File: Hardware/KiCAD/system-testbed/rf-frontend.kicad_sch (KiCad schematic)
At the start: 42 parts

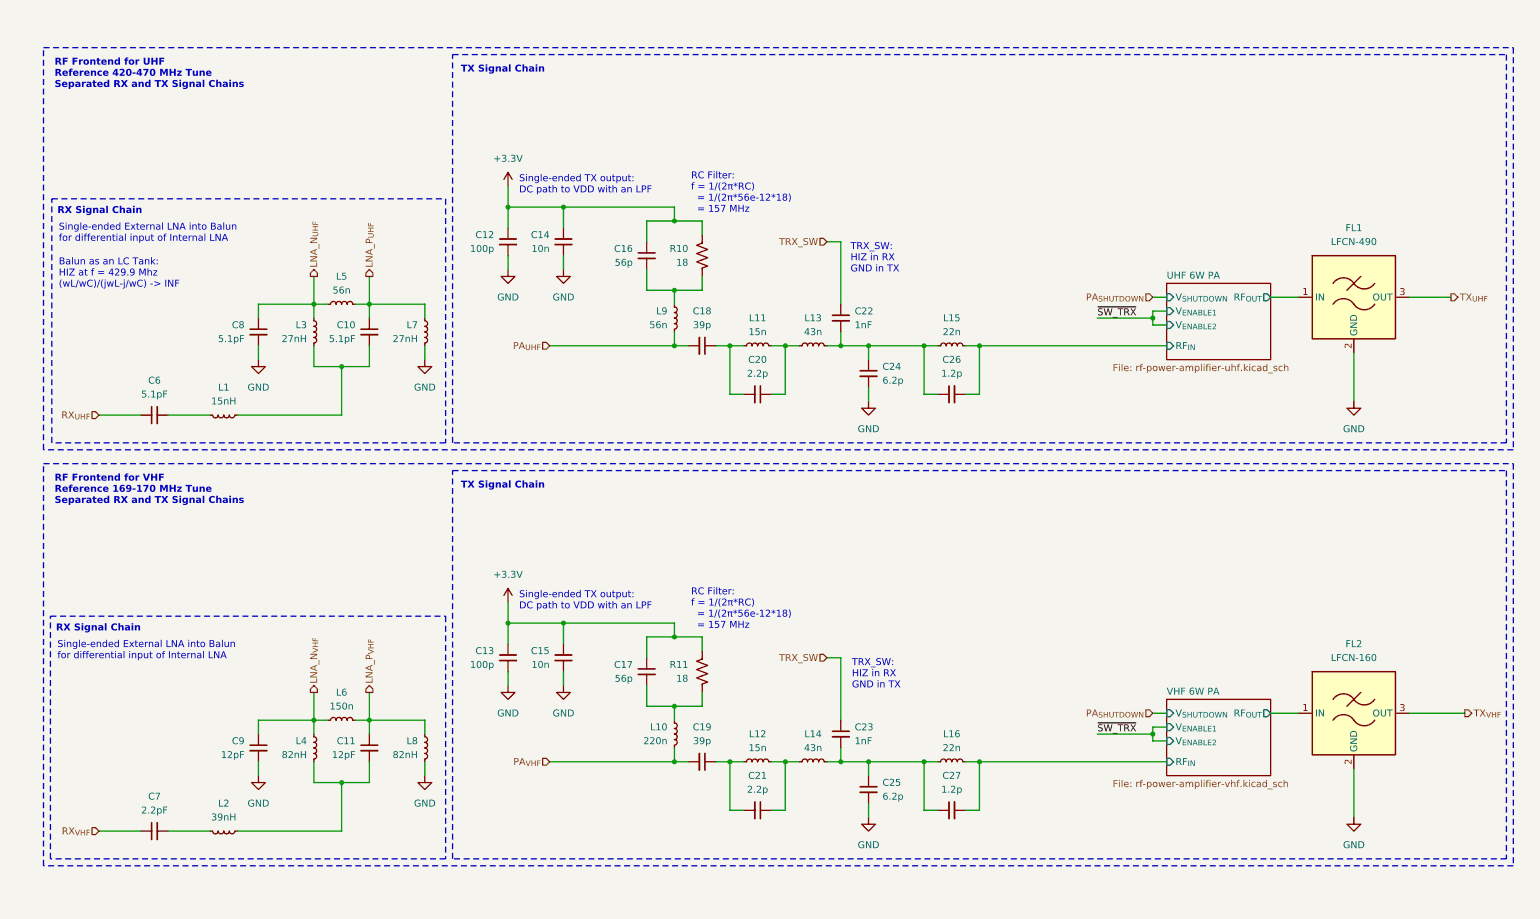
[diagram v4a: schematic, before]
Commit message: feat: separate RF subsystems for testing using SMA edge launches in testbed KiCAD project #65 #34 #45
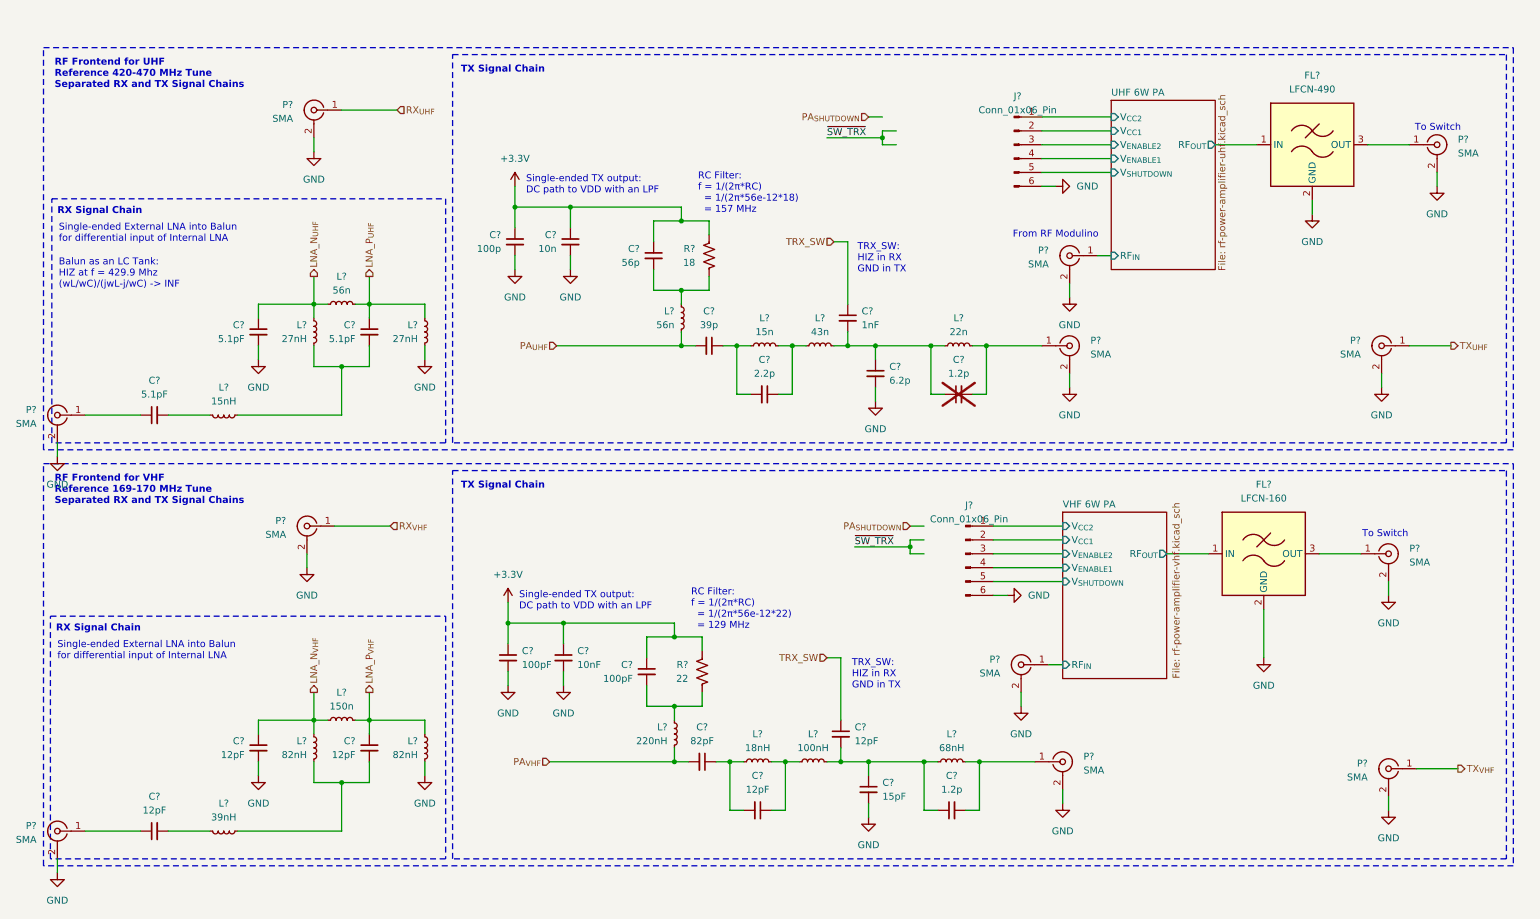
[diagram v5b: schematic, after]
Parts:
- added J? (x2): Conn_01x06_Pin, Connector_PinHeader_2.54mm:PinHeader_1x06_P2.54mm_Vertical, symbol Connector:Conn_01x06_Pin
- added P? (x12): SMA, Connector_Coaxial:SMA_Molex_73251-1153_EdgeMount_Horizontal, symbol Connector:Conn_Coaxial
- C?: renamed from C26; now not fitted
- C?: renamed from C19; value 39p -> 82pF
- C?: renamed from C17; value 56p -> 100pF
- C?: renamed from C21; value 2.2p -> 12pF
- C?: renamed from C15; value 10n -> 10nF
- C?: renamed from C7; value 2.2pF -> 12pF
- C?: renamed from C13; value 100p -> 100pF
- C?: renamed from C25; value 6.2p -> 15pF
- C?: renamed from C23; value 1nF -> 12pF
- C?: renamed from C6; footprint Capacitor_SMD:C_0603_1608Metric -> Capacitor_SMD:C_0402_1005Metric
- L?: renamed from L12; value 15n -> 18nH
- L?: renamed from L14; value 43n -> 100nH
- L?: renamed from L16; value 22n -> 68nH
- L?: renamed from L10; value 220n -> 220nH
- R?: renamed from R11; value 18 -> 22
- renumbered C18 to C?, C9 to C?, C22 to C?, C16 to C?, C8 to C?, C14 to C?, C20 to C?, C12 to C?, C27 to C?, C11 to C?, C24 to C?, C10 to C?, FL1 to FL?, FL2 to FL?, L13 to L?, L7 to L?, L8 to L?, L4 to L?, L9 to L?, L6 to L?, L2 to L?, L11 to L?, L3 to L?, L1 to L?, L15 to L?, L5 to L?, R10 to R?
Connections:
- net GND: now also J?.6 (Pin_6), J?.6 (Pin_6), P?.2 (Ext), P?.2 (Ext), P?.2 (Ext), P?.2 (Ext), P?.2 (Ext), P?.2 (Ext), P?.2 (Ext), P?.2 (Ext), P?.2 (Ext), P?.2 (Ext), P?.2 (Ext), P?.2 (Ext)
- net RX_{UHF}: now also P?.1 (In); no longer C?.1
- net RX_{VHF}: now also P?.1 (In); no longer C?.1
- net TX_{UHF}: now also P?.1 (In); no longer FL?.3 (OUT)
- net TX_{VHF}: now also P?.1 (In); no longer FL?.3 (OUT)
- net UHF 6W PA/RF_{IN}: now also P?.1 (In); no longer C?.2, L?.2
- net VHF 6W PA/RF_{IN}: now also P?.1 (In); no longer C?.2, L?.2
- new net: C?.2, L?.2, P?.1 (In) (x2)
- new net: FL?.3 (OUT), P?.1 (In) (x2)
- new net: C?.1, P?.1 (In) (x2)
- new net UHF 6W PA/V_{CC1}: J?.2 (Pin_2)
- new net UHF 6W PA/V_{CC2}: J?.1 (Pin_1)
- new net UHF 6W PA/V_{ENABLE1}: J?.4 (Pin_4)
- new net UHF 6W PA/V_{ENABLE2}: J?.3 (Pin_3)
- new net UHF 6W PA/V_{SHUTDOWN}: J?.5 (Pin_5)
- new net VHF 6W PA/V_{CC1}: J?.2 (Pin_2)
- new net VHF 6W PA/V_{CC2}: J?.1 (Pin_1)
- new net VHF 6W PA/V_{ENABLE1}: J?.4 (Pin_4)
- new net VHF 6W PA/V_{ENABLE2}: J?.3 (Pin_3)
- new net VHF 6W PA/V_{SHUTDOWN}: J?.5 (Pin_5)
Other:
- sheet UHF 6W PA ports: added V_{CC1}, V_{CC2}; removed none
- sheet VHF 6W PA ports: added V_{CC1}, V_{CC2}; removed none
- note added: "From RF Modulino"
- note added: "RC Filter: f = 1/(2π*RC) = 1/(2π*56e-12*22) = 129 MHz"
- note added: "To Switch"
- moved on the sheet: C?, FL?, L?, R?
